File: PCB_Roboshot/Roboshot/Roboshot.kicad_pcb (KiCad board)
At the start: 2 copper layers, 63.3 x 86 mm, 35 parts, among them J1 Conn_01x08, Q1_LIGHT1 BC546, SW1 SW_Push_Dual_x2, U1 7840-0000PR, U2 H

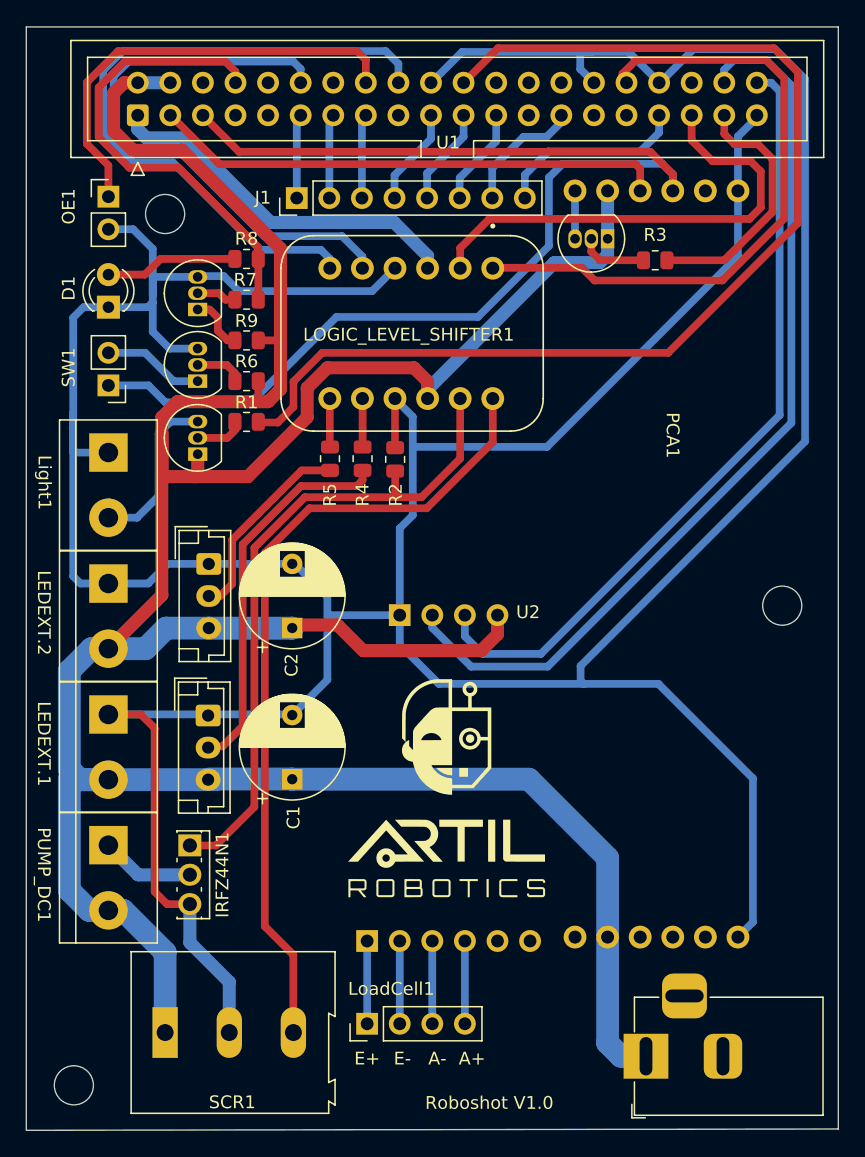
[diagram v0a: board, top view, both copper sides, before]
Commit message: Defini Valores en resistencia y arregle el problema el InvPin en el boton de Power
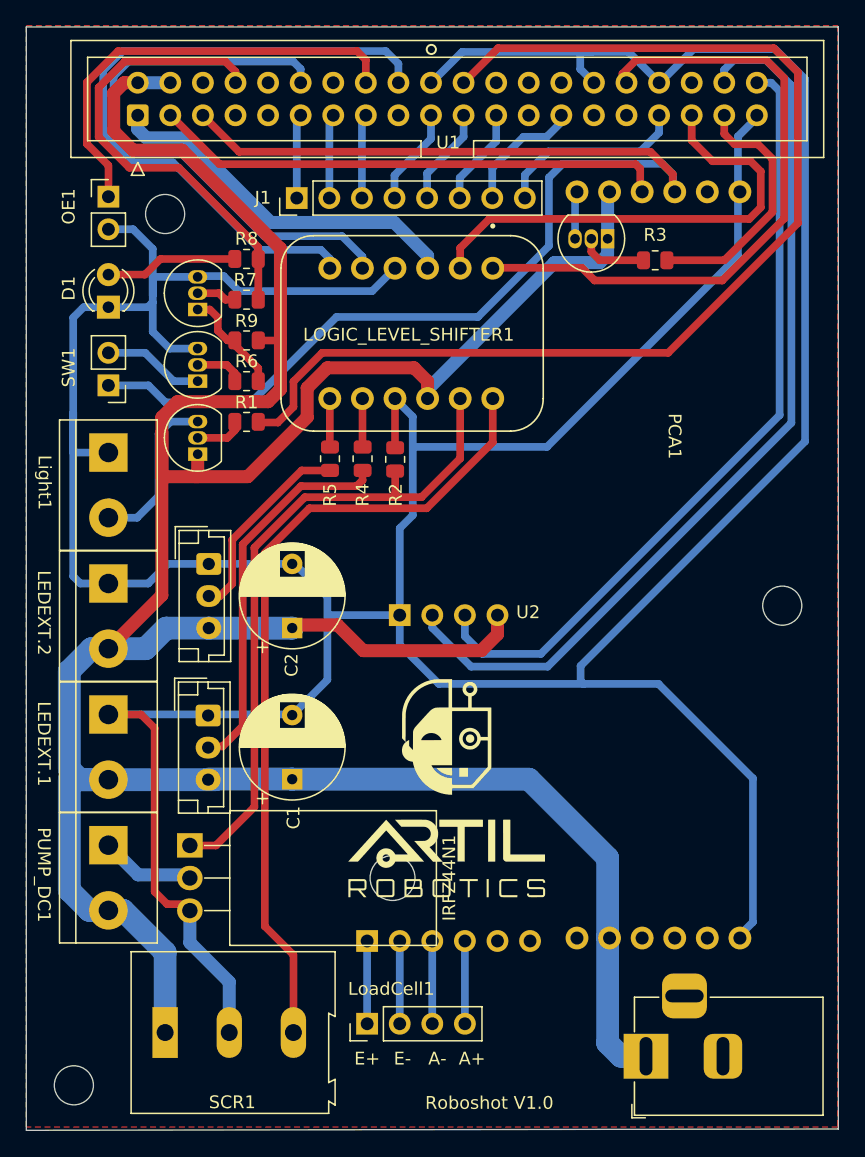
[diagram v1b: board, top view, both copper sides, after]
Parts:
- IRFZ44N1: footprint Package_TO_SOT_THT:SIPAK_Vertical -> Package_TO_SOT_THT:TO-220F-3_Horizontal_TabDown
- moved PCA1 0.17 mm to (124.7, 133.3)
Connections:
- BUTTON1 pad 1: Net-(BUTTON1-Pad1) -> /Inv.OUPUT
- R6 pad 1: +5V -> /Inv.OUPUT
- R9 pad 1: Net-(BUTTON1-Pad1) -> /Inv.OUPUT
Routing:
- net /Inv.OUPUT: track 0.00 -> 8.43 mm
- net Net-(BUTTON1-Pad1): track 4.50 -> 0.00 mm
- net +5V: track 265.1 -> 263.7 mm
- added copper zone on F.Cu, net +5V
